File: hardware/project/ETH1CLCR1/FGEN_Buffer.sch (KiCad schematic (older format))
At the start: 57 parts, among them K1001 9012, K1002 9012, K1003 9012, K1004 9012, Q1001 MMBT4401L, Q1002 MMBT4403L, Q1003 BC847W, Q1004 BC847W, Q1005 BC847W, Q1006 BC847W, U1001 TL072, U1002 LT1468, U1003 AQY212GS, U1004 AD5293BRUZ-20

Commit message: PCB layout
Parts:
- D1003, D1004: footprint Diode_SMD:D_SMA_Handsoldering -> Diode_SMD:D_SMA
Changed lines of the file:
@@
 F 0 "D1003" V 6954 4029 50  0000 L CNN
 F 1 "SML4757A" V 7045 4029 50  0000 L CNN
-F 2 "Diode_SMD:D_SMA_Handsoldering" H 7000 3950 50  0001 C CNN
+F 2 "Diode_SMD:D_SMA" H 7000 3950 50  0001 C CNN
 F 3 "~" H 7000 3950 50  0001 C CNN
 	1    7000 3950
@@
 F 0 "D1004" V 7046 4221 50  0000 R CNN
 F 1 "SML4757A" V 6955 4221 50  0000 R CNN
-F 2 "Diode_SMD:D_SMA_Handsoldering" H 7000 4300 50  0001 C CNN
+F 2 "Diode_SMD:D_SMA" H 7000 4300 50  0001 C CNN
 F 3 "~" H 7000 4300 50  0001 C CNN
 	1    7000 4300

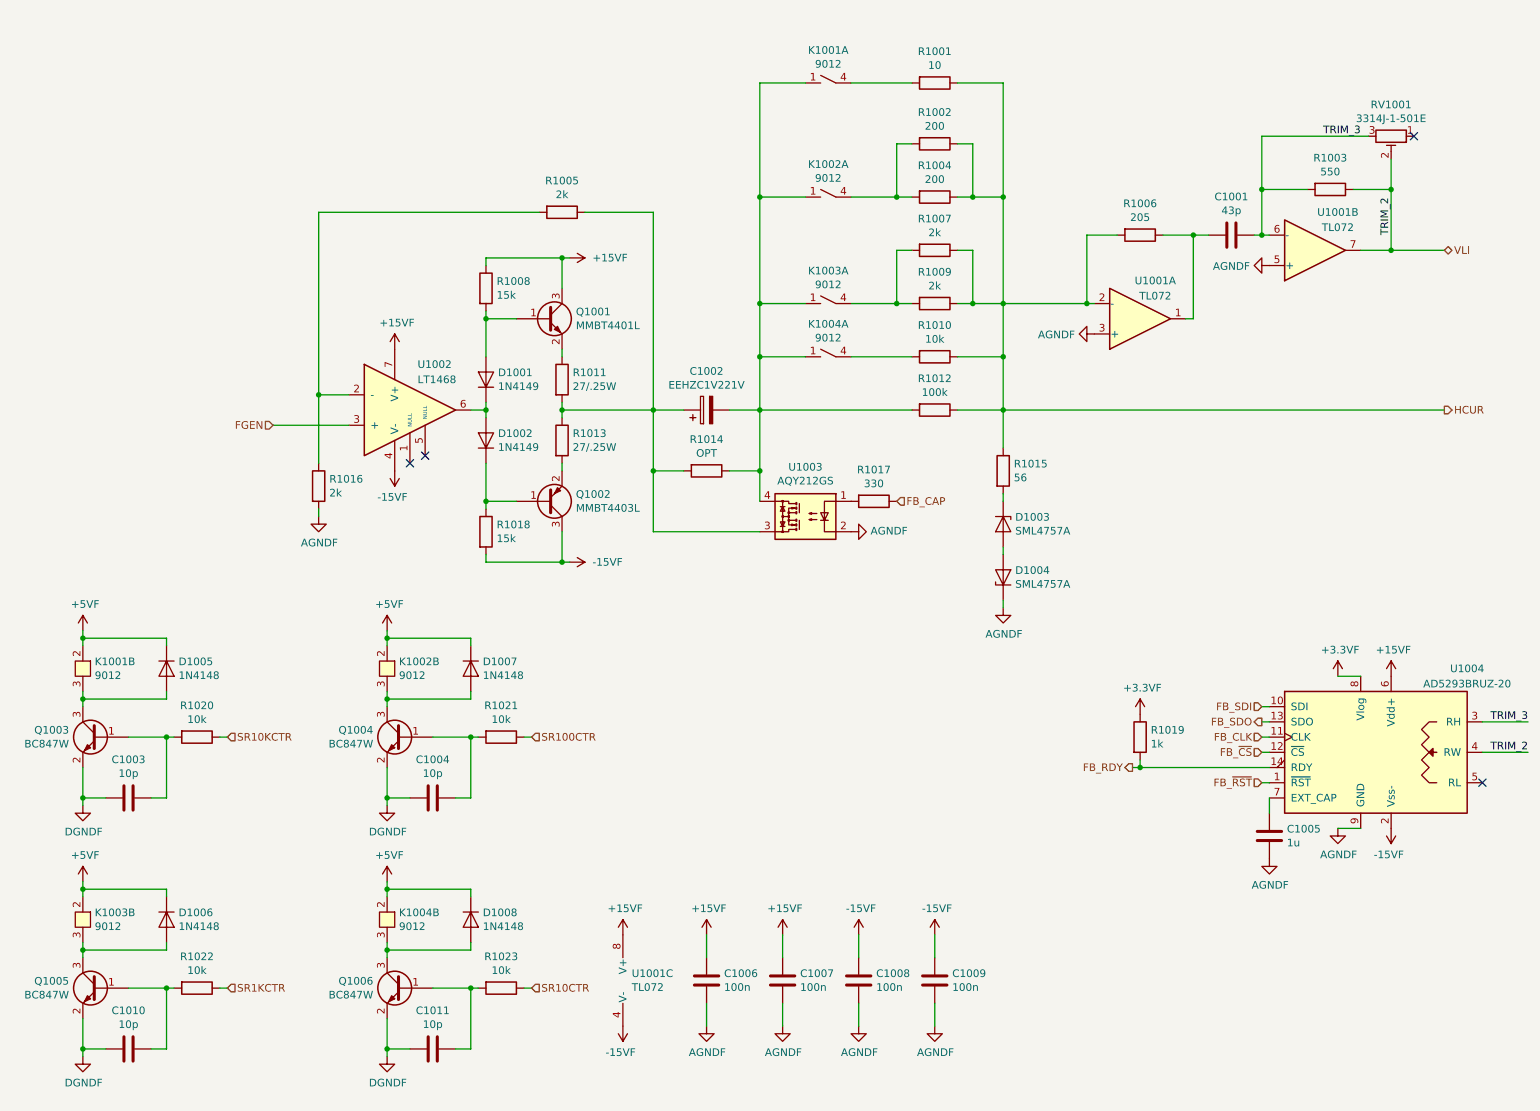
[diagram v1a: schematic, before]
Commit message: Redesinged ADC schematic.
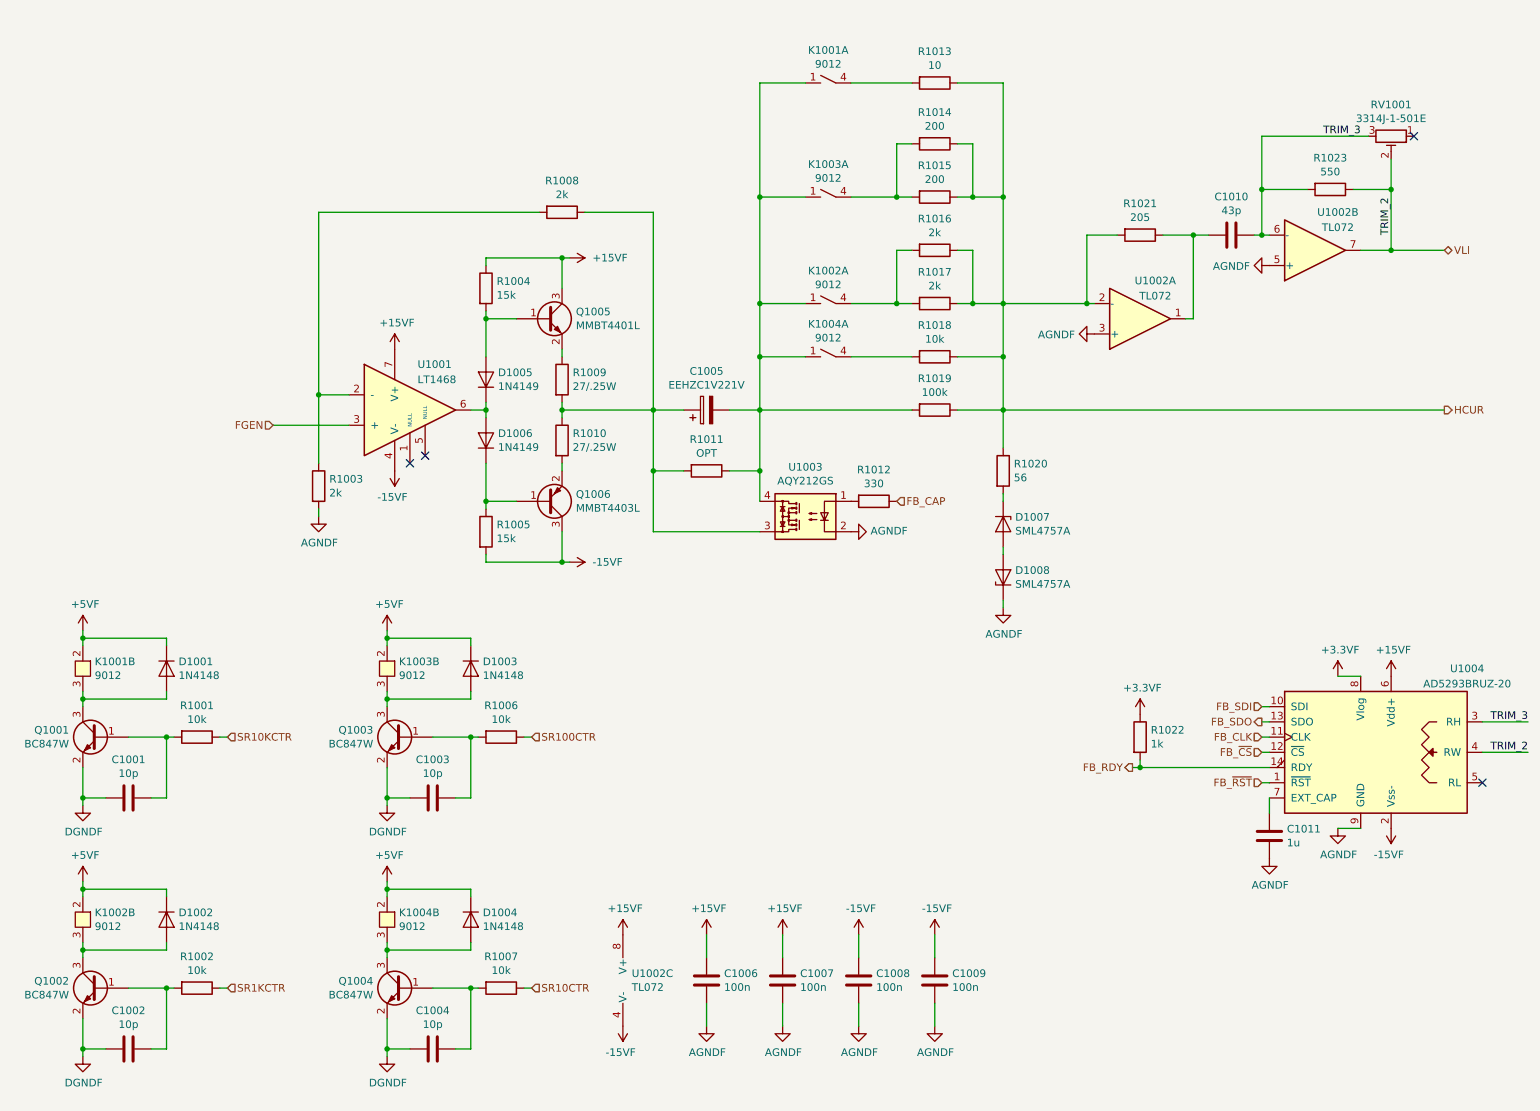
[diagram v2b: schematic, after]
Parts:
- renumbered C1003 to C1001, C1010 to C1002, C1004 to C1003, C1011 to C1004, C1002 to C1005, C1001 to C1010, C1005 to C1011, D1005 to D1001, D1006 to D1002, D1007 to D1003, D1008 to D1004, D1001 to D1005, D1002 to D1006, D1003 to D1007, D1004 to D1008, K1003 to K1002, K1002 to K1003, Q1003 to Q1001, Q1005 to Q1002, Q1004 to Q1003, Q1006 to Q1004, Q1001 to Q1005, Q1002 to Q1006, R1020 to R1001, R1022 to R1002, R1016 to R1003, R1008 to R1004, R1018 to R1005, R1021 to R1006, R1023 to R1007, R1005 to R1008, R1011 to R1009, R1013 to R1010, R1014 to R1011, R1017 to R1012, R1001 to R1013, R1002 to R1014, R1004 to R1015, R1007 to R1016, R1009 to R1017, R1010 to R1018, R1012 to R1019, R1015 to R1020, R1006 to R1021, R1019 to R1022, R1003 to R1023, U1002 to U1001, U1001 to U1002

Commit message: Redesigned the power supply, added humidy+temp. sensor.
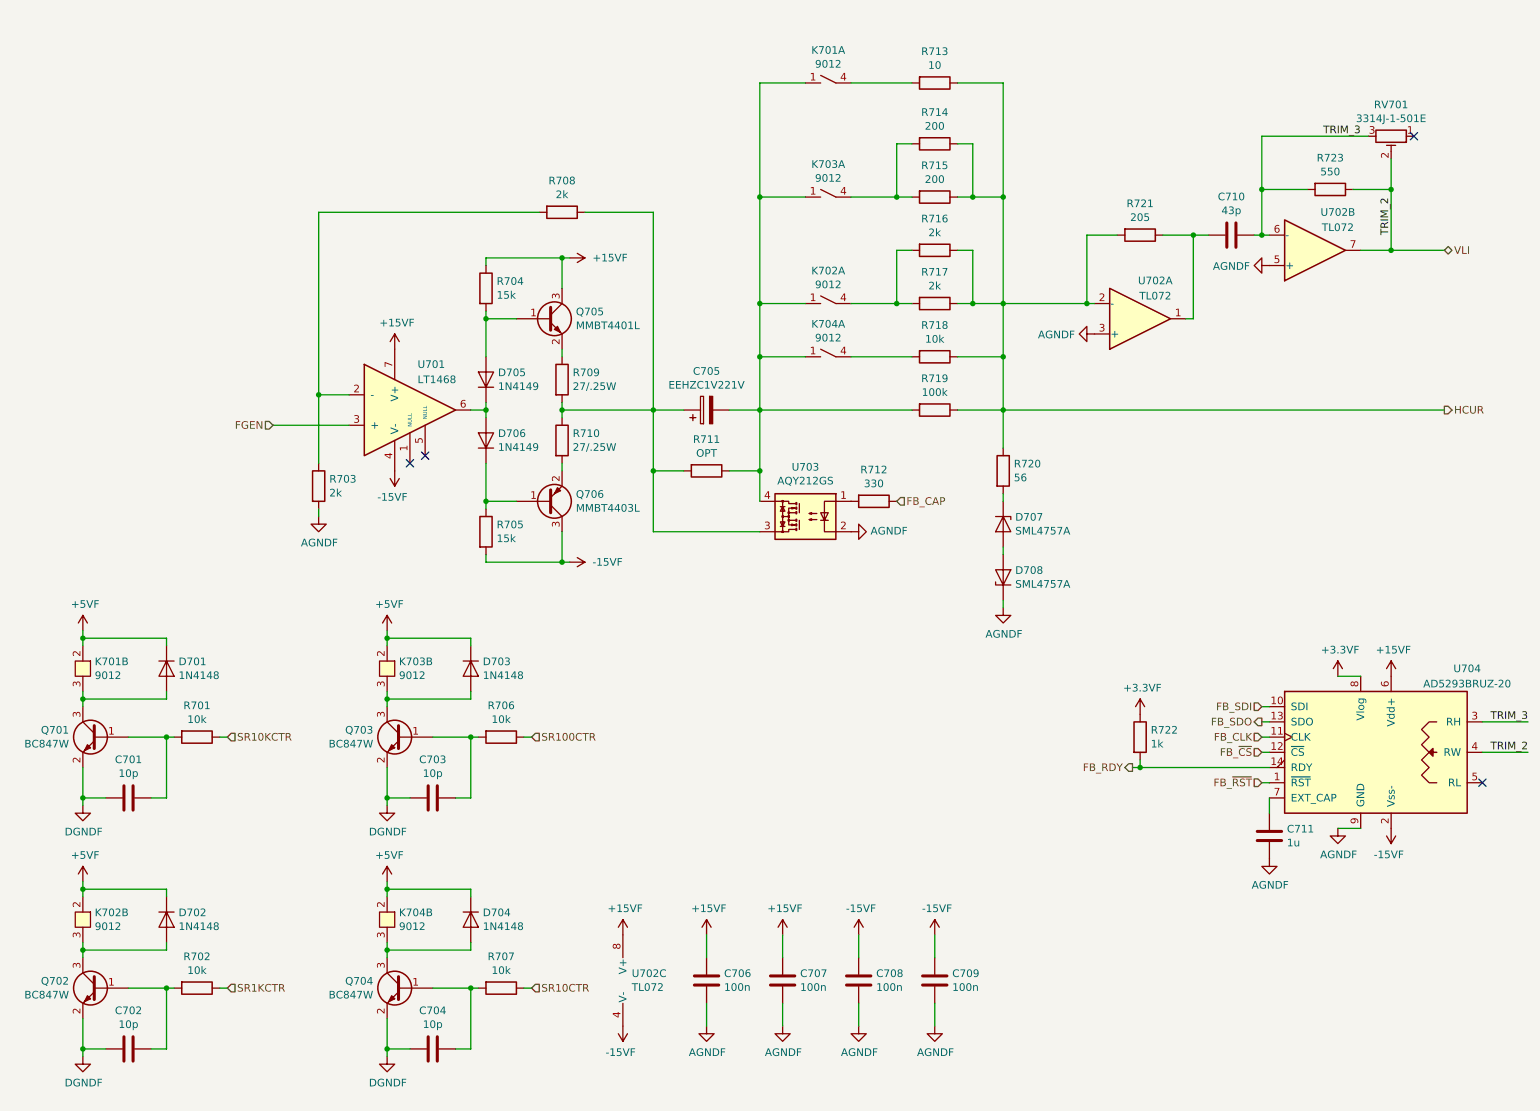
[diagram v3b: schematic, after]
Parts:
- renumbered C1001 to C701, C1002 to C702, C1003 to C703, C1004 to C704, C1005 to C705, C1006 to C706, C1007 to C707, C1008 to C708, C1009 to C709, C1010 to C710, C1011 to C711, D1001 to D701, D1002 to D702, D1003 to D703, D1004 to D704, D1005 to D705, D1006 to D706, D1007 to D707, D1008 to D708, K1001 to K701, K1002 to K702, K1003 to K703, K1004 to K704, Q1001 to Q701, Q1002 to Q702, Q1003 to Q703, Q1004 to Q704, Q1005 to Q705, Q1006 to Q706, R1001 to R701, R1002 to R702, R1003 to R703, R1004 to R704, R1005 to R705, R1006 to R706, R1007 to R707, R1008 to R708, R1009 to R709, R1010 to R710, R1011 to R711, R1012 to R712, R1013 to R713, R1014 to R714, R1015 to R715, R1016 to R716, R1017 to R717, R1018 to R718, R1019 to R719, R1020 to R720, R1021 to R721, R1022 to R722, R1023 to R723, RV1001 to RV701, U1001 to U701, U1002 to U702, U1003 to U703, U1004 to U704

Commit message: PCB layout
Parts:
- added C712: 100n, Capacitor_SMD:C_0603_1608Metric_Pad1.05x0.95mm_HandSolder, symbol Device:C
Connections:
- net +3.3VF: now also C712.1
- net AGNDF: now also C712.2
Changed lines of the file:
@@
 	-1   0    0    1
 $EndComp
+$Comp
+L Device:C C712
+U 1 1 5E6471EB
+P 5050 5900
+F 0 "C712" H 5165 5946 50  0000 L CNN
+F 1 "100n" H 5165 5855 50  0000 L CNN
+F 2 "Capacitor_SMD:C_0603_1608Metric_Pad1.05x0.95mm_HandSolder" H 5088 5750 50  0001 C CNN
+F 3 "~" H 5050 5900 50  0001 C CNN
+	1    5050 5900
+	1    0    0    -1
+$EndComp
+$Comp
+L ETH1CLCR1:AGNDF #PWR0106
+U 1 1 5E6471F1
+P 5050 6200
+F 0 "#PWR0106" H 5050 5950 50  0001 C CNN
+F 1 "AGNDF" H 5055 6027 50  0000 C CNN
+F 2 "" H 5050 6200 50  0001 C CNN
+F 3 "" H 5050 6200 50  0001 C CNN
+	1    5050 6200
+	1    0    0    -1
+$EndComp
+Wire Wire Line
+	5050 6050 5050 6200
+Wire Wire Line
+	5050 5750 5050 5600
+$Comp
+L ETH1CLCR1:+3.3VF #PWR0107
+U 1 1 5E651F2D
+P 5050 5600
+F 0 "#PWR0107" H 5050 5450 50  0001 C CNN
+F 1 "+3.3VF" H 5065 5773 50  0000 C CNN
+F 2 "" H 5050 5600 50  0001 C CNN
+F 3 "" H 5050 5600 50  0001 C CNN
+	1    5050 5600
+	1    0    0    -1
+$EndComp
 $EndSCHEMATC

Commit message: Changes in schematics.
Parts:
- removed Q701, Q702, Q703, Q704: BC847W, Package_TO_SOT_SMD:SOT-323_SC-70, symbol Transistor_BJT:BC847W
- added C705, C706: 100n, Capacitor_SMD:C_0603_1608Metric_Pad1.05x0.95mm_HandSolder, symbol Device:C
- added Q701, Q702, Q703, Q704: BC847, Package_TO_SOT_SMD:SOT-23, symbol Transistor_BJT:BC847
- C713: renamed from C710; value 43p -> 43p/300V
- R722: value 1k -> 2k2
- renumbered C712 to C707, C705 to C708, C706 to C709, C707 to C710, C708 to C711, C709 to C712, C711 to C714, R706 to R704, R707 to R705, R704 to R706, R705 to R707
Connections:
- net +15VF: now also C705.1
- net -15VF: now also C706.1
- net AGNDF: now also C705.2, C706.2
- net DGNDF: now also Q701.2 (E), Q702.2 (E), Q703.2 (E), Q704.2 (E)
- net at C701.1, R701.2: now also Q701.1 (B)
- net at D701.2 (A), K701.3: now also Q701.3 (C)
- net at C702.1, R702.2: now also Q702.1 (B)
- net at D702.2 (A), K702.3: now also Q702.3 (C)
- net at C703.1, R704.2: now also Q703.1 (B)
- net at D703.2 (A), K703.3: now also Q703.3 (C)
- net at C704.1, R705.2: now also Q704.1 (B)
- net at D704.2 (A), K704.3: now also Q704.3 (C)
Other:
- moved on the sheet: C701, C702, C703, C704, C707, C709, C710, C711, C713, D701, D702, D703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

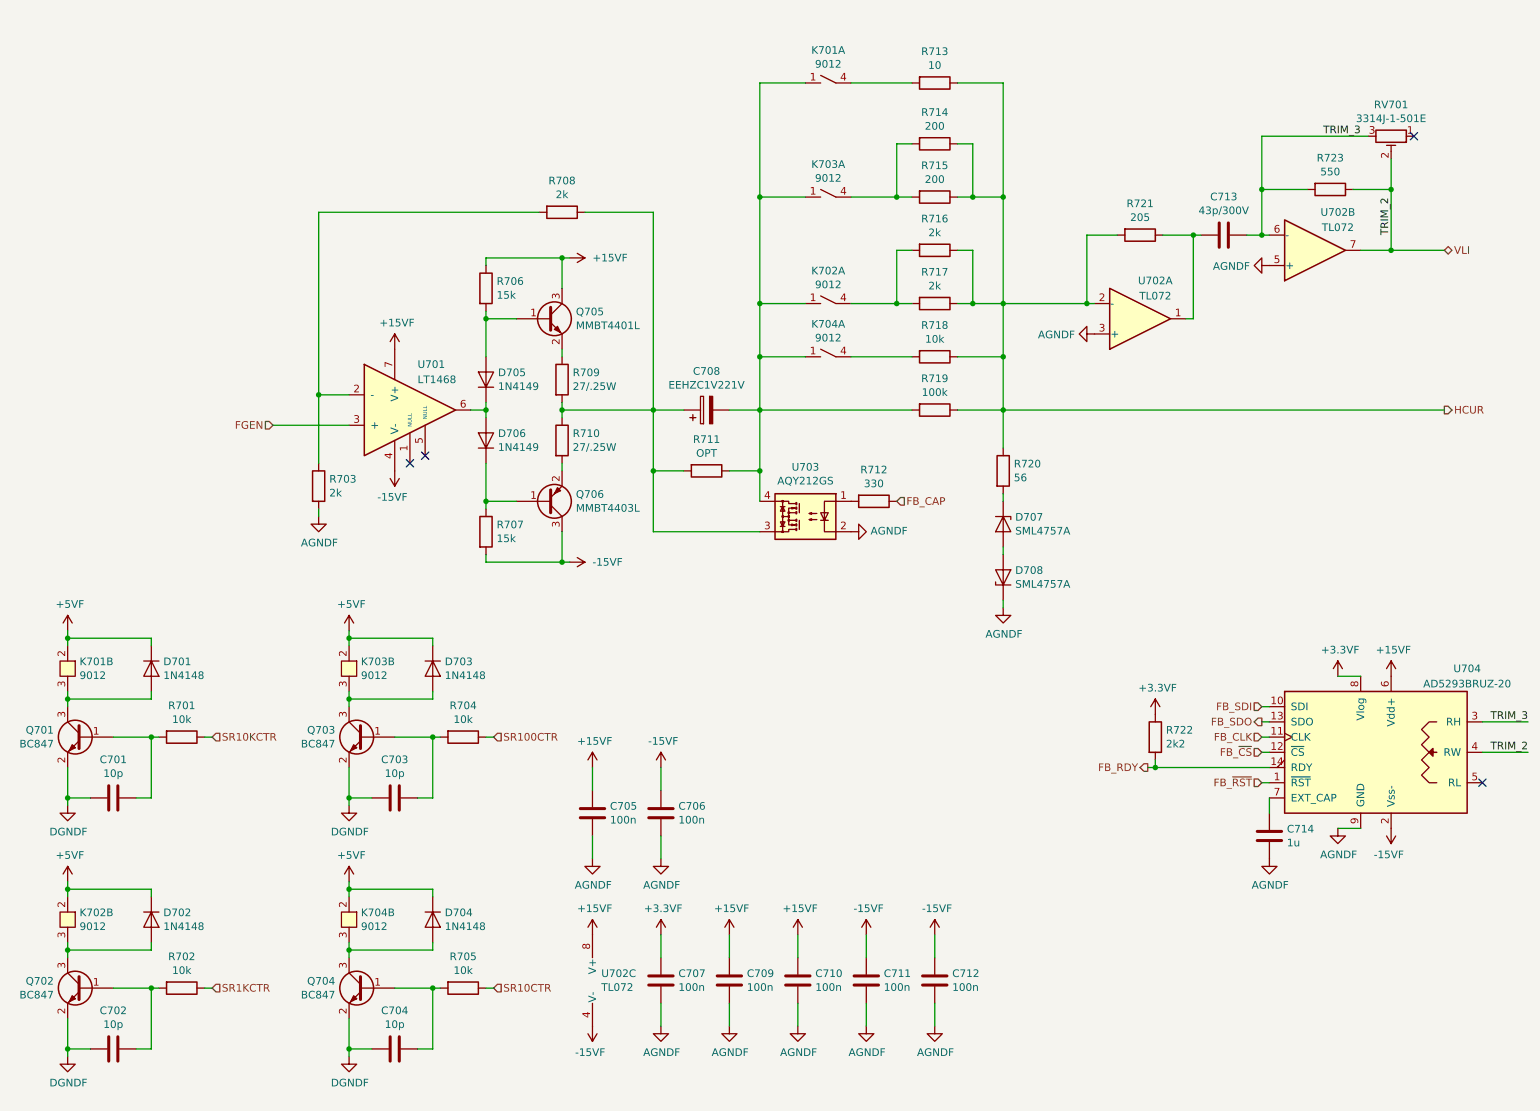
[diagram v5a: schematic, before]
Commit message: Checked the schematics. Created BOM.
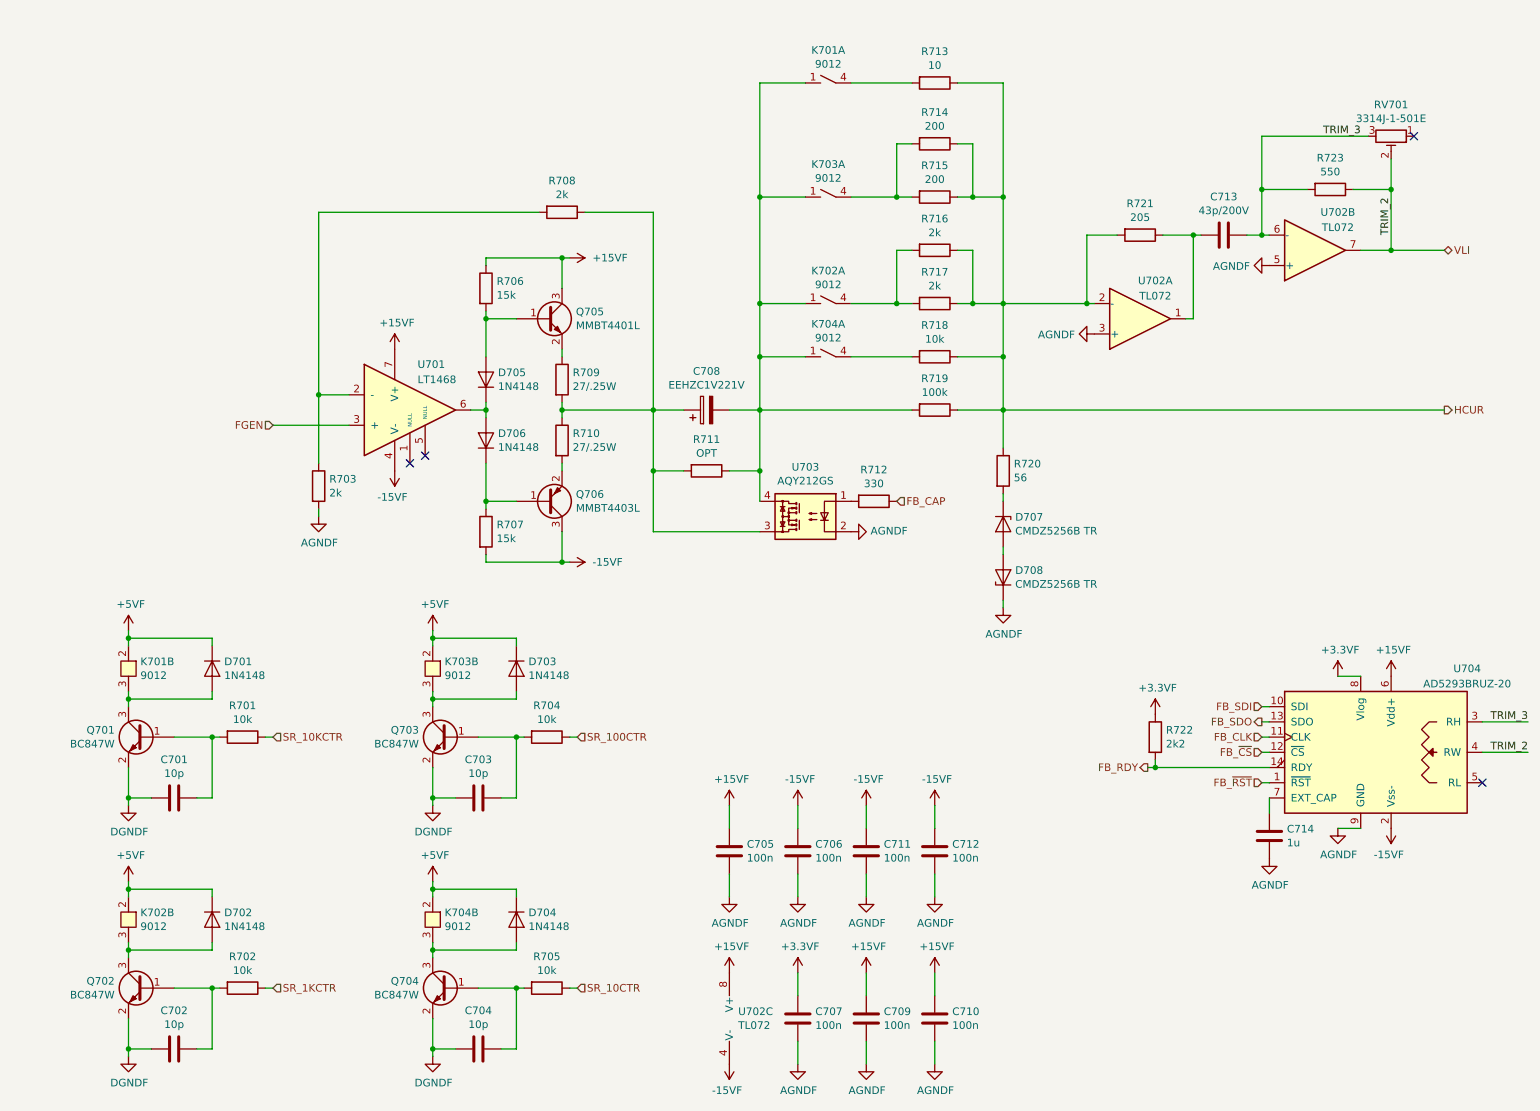
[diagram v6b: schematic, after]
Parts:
- removed Q701, Q702, Q703, Q704: BC847, Package_TO_SOT_SMD:SOT-23, symbol Transistor_BJT:BC847
- added Q701, Q702, Q703, Q704: BC847W, Package_TO_SOT_SMD:SOT-323_SC-70, symbol Transistor_BJT:BC847W
- C713: value 43p/300V -> 43p/200V
- D705, D706: value 1N4149 -> 1N4148
- D707, D708: value SML4757A -> CMDZ5256B TR; footprint Diode_SMD:D_SMA -> Diode_SMD:D_SOD-323_HandSoldering
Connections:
- net DGNDF: now also Q701.2 (E), Q702.2 (E), Q703.2 (E), Q704.2 (E)
- net at C701.1, R701.2: now also Q701.1 (B)
- net at C702.1, R702.2: now also Q702.1 (B)
- net at C703.1, R704.2: now also Q703.1 (B)
- net at C704.1, R705.2: now also Q704.1 (B)
- net at D701.2 (A), K701.3: now also Q701.3 (C)
- net at D703.2 (A), K703.3: now also Q703.3 (C)
- net at D702.2 (A), K702.3: now also Q702.3 (C)
- net at D704.2 (A), K704.3: now also Q704.3 (C)
- net SR100CTR renamed SR_100CTR
- net SR10CTR renamed SR_10CTR
- net SR10KCTR renamed SR_10KCTR
- net SR1KCTR renamed SR_1KCTR
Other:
- moved on the sheet: C701, C702, C703, C704, C705, C706, C707, C709, C710, C711, C712, D701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
